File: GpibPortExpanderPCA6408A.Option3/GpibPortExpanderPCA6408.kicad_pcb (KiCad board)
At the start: 2 copper layers, 39 parts, among them J1 DEBUG_CON_01X08, J2 GPIB_CON_9P, J3 GPIB_CON_9P, J4 SATA_PLUG_CON_14P, U1 PCA6416A

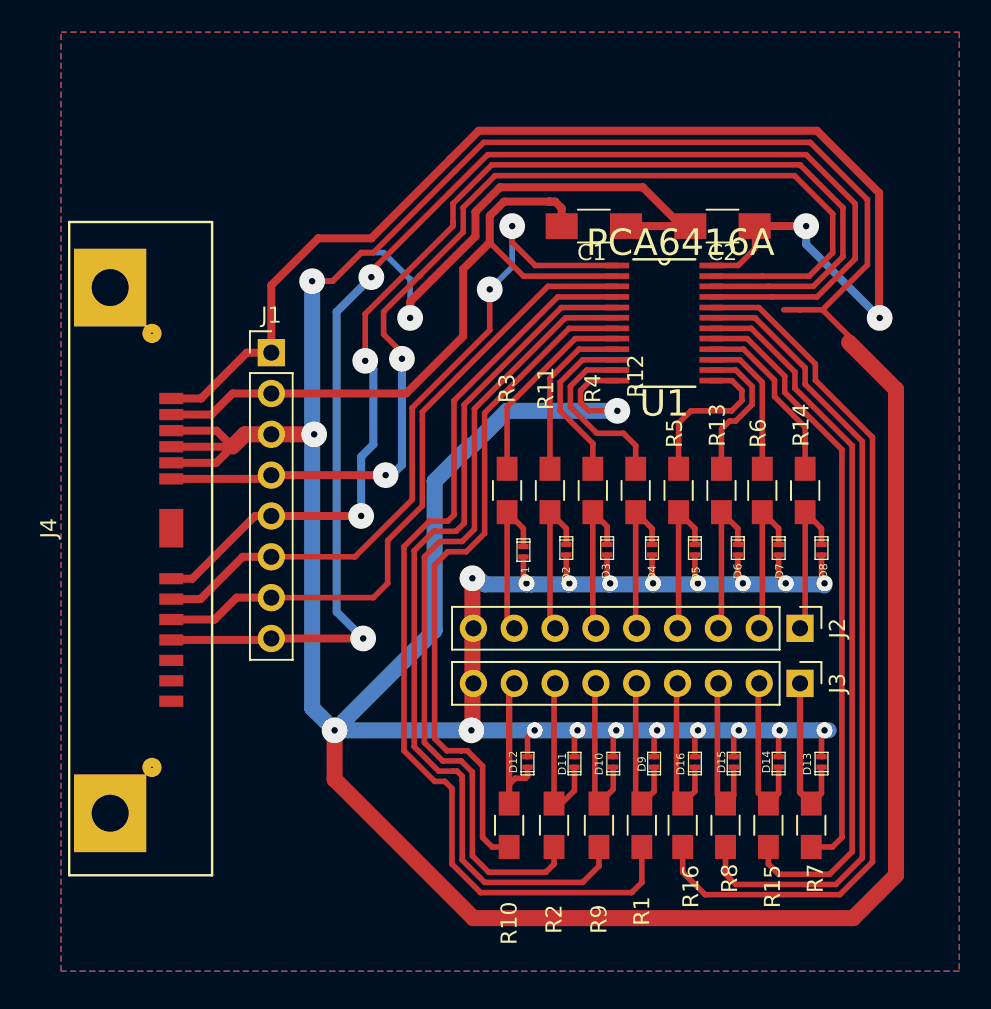
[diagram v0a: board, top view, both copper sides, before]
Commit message: Revision de PCBs + MergedPcbs
  - Se revisan PCBs
      - VikingPortExpander
      - GpibPortExpander
      - MainBoards en tres versiones
  - Se genera archivos Gerber que combina estos PCBs en un documento
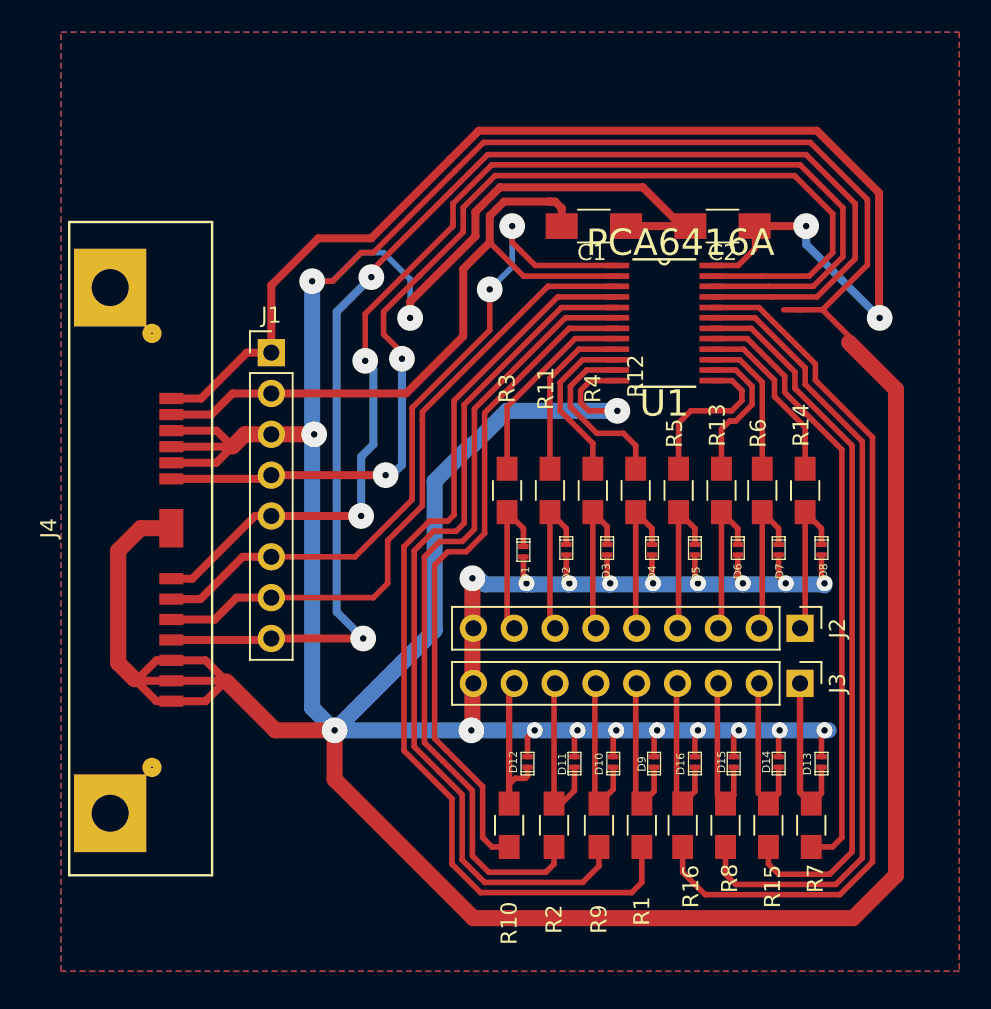
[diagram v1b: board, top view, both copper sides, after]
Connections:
- J4 pad 11: Net-(J4-Pad11) -> GND
- J4 pad 12: Net-(J4-Pad12) -> GND
- J4 pad 13: Net-(J4-Pad13) -> GND
- J4 pad 14: Net-(J4-Pad14) -> GND
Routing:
- net GND: track 342.3 -> 381.6 mm
- net Net-(R10-Pad2): track 42.7 -> 41.9 mm
- net Net-(R2-Pad2): track 49.8 -> 49.2 mm
- net Net-(R9-Pad2): track 55.1 -> 54.4 mm

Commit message: Revision de PCbs + generacion de nuevos archivos Gerber
  - Se corrigen pads de pin headers
  - Se revisan
  - MainBoard option 2
  - PortExpander MC33996.Option3
  - GpibPortExpanderPCA6408A.Option3
  - Se generan Gerber + Vistas 3D
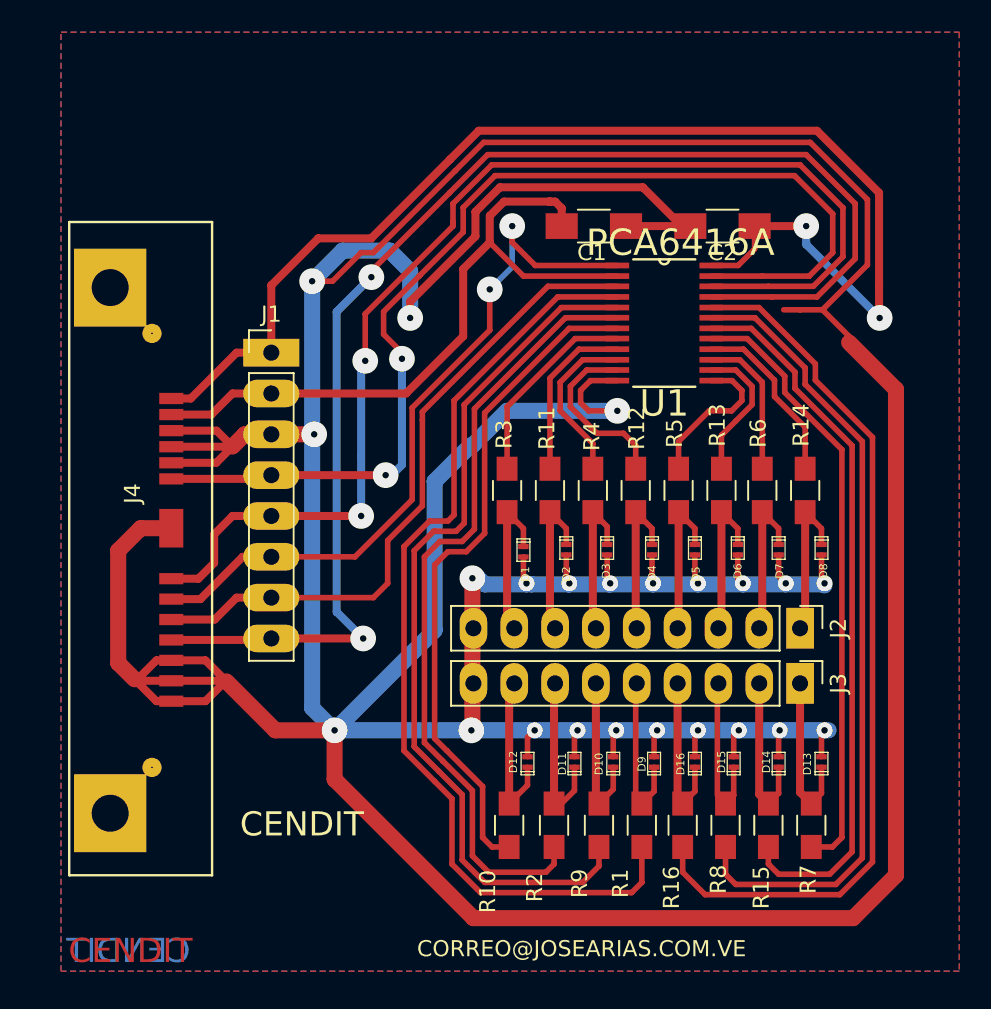
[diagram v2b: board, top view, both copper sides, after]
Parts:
- J1: footprint Pin_Headers:Pin_Header_Straight_1x08_Pitch2.54mm -> CenditFootprints:DEBUG_CON_8P
- J2, J3: footprint Pin_Headers:Pin_Header_Straight_1x09_Pitch2.54mm -> CenditFootprints:GPIB_HEADER_9P
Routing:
- net /SCL: track 74.0 -> 75.6 mm
- net /REN: track 10.7 -> 12.0 mm
- net /DAV: track 9.56 -> 10.2 mm
- net Net-(R5-Pad2): track 10.1 -> 9.48 mm
- net /D0: track 9.87 -> 10.5 mm
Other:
- board text added: "CENDIT"
- board text added: "CORREO@JOSEARIAS.COM.VE"
